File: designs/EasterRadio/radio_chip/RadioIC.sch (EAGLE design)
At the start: 28 parts, among them Q1 2SC3838T146, Y1 32.768kHz crystal

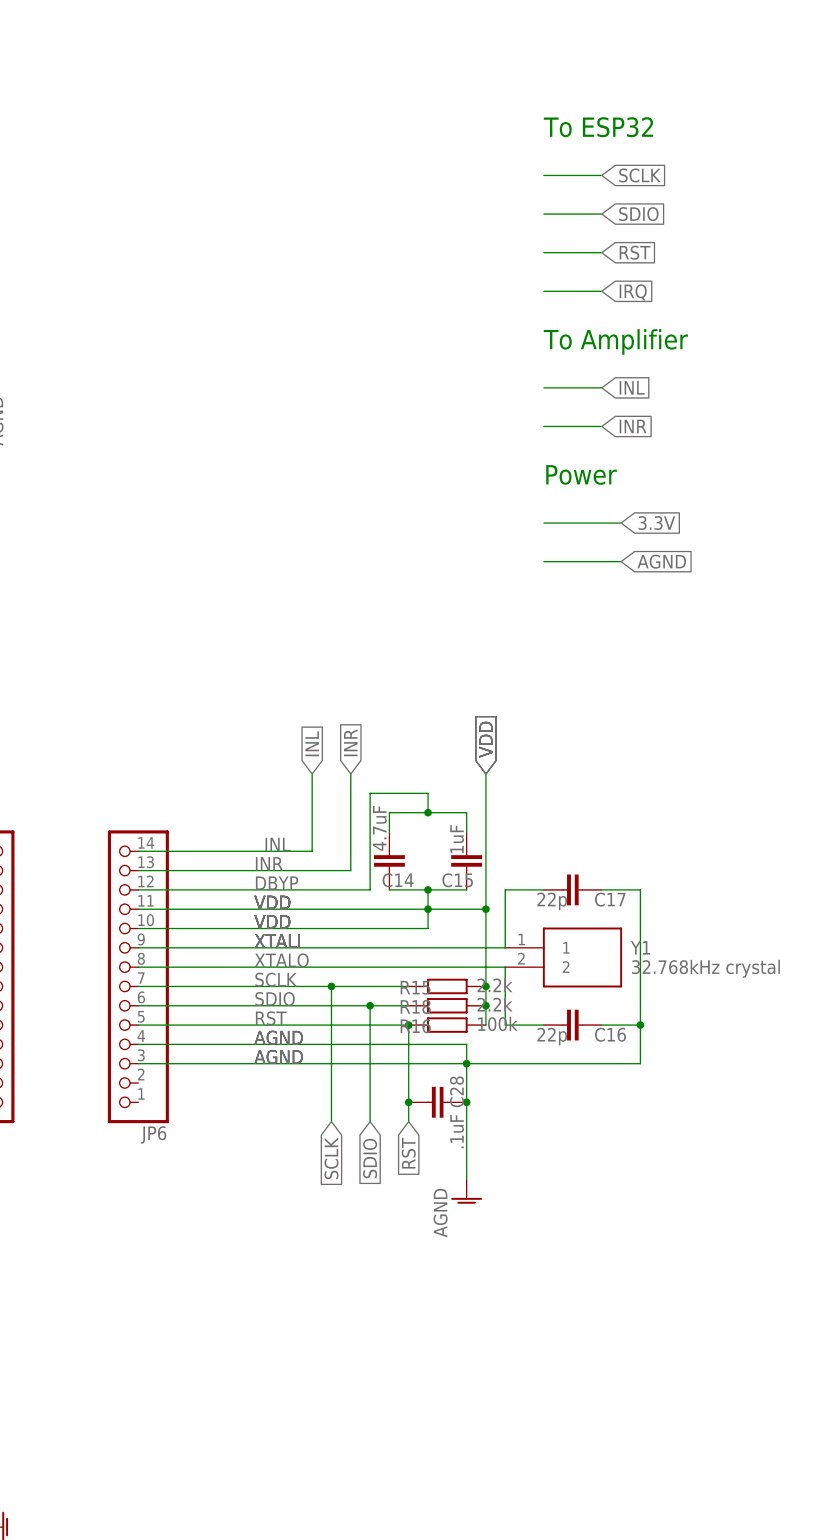
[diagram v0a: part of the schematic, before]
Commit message: changed radio IC
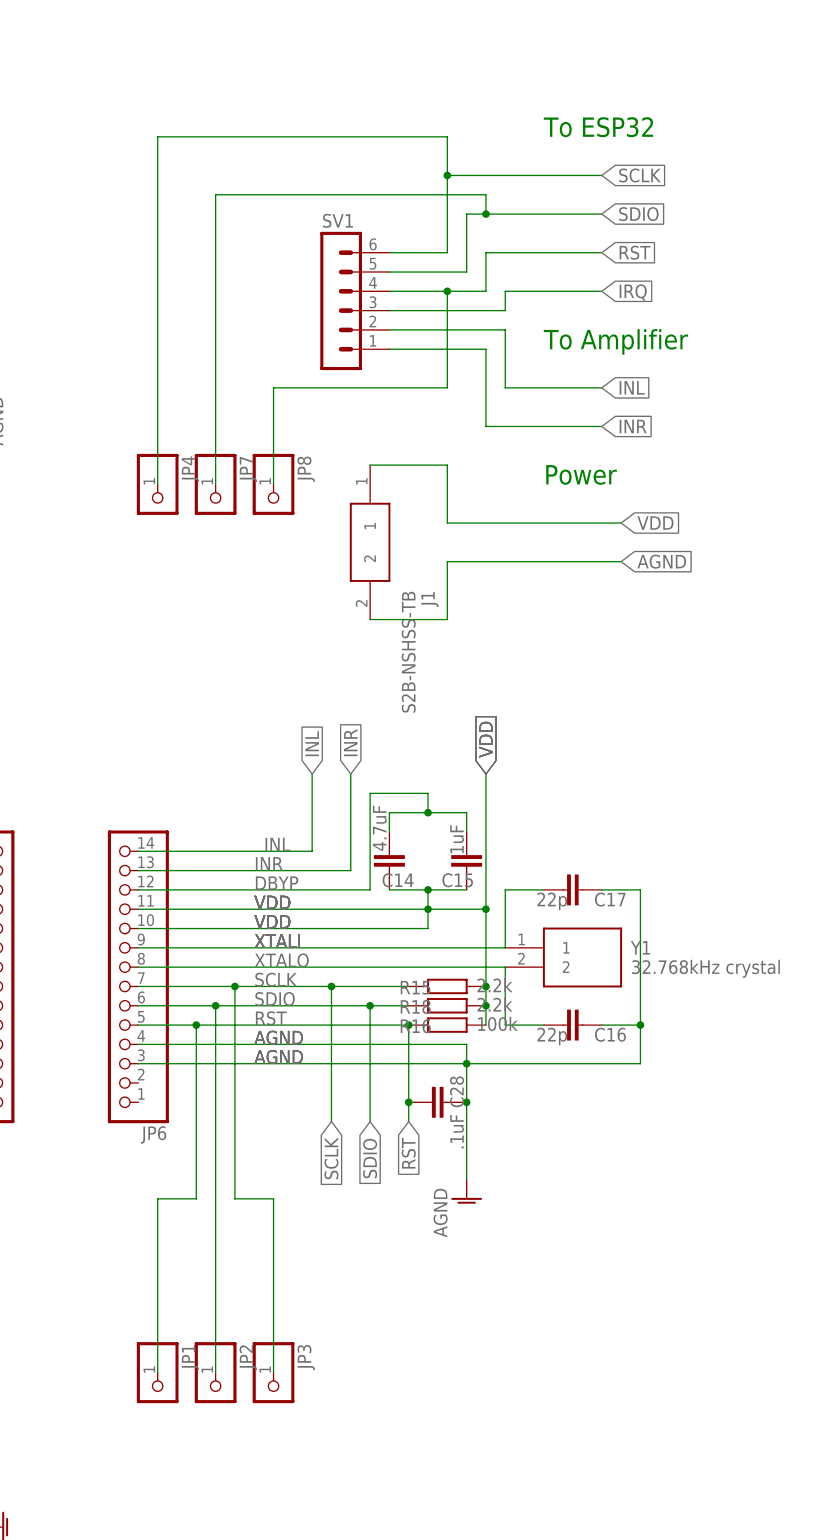
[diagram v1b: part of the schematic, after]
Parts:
- added J1: S2B-NSHSS-TB, CommonParts:S2B-NSHSS-TB
- added JP1, JP2, JP3, JP4, JP7, JP8: (no value), pinhead:PINHD-1X1
- added SV1: (no value), con-lstb:MA06-1
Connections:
- net AGND: now also J1.2
- net INL: now also SV1.2
- net INR: now also SV1.1
- net IRQ: now also SV1.3
- net RST: now also JP1.1, JP8.1, SV1.4
- net SCLK: now also JP3.1, JP4.1, SV1.6
- net SDIO: now also JP2.1, JP7.1, SV1.5
- net VDD: now also J1.1

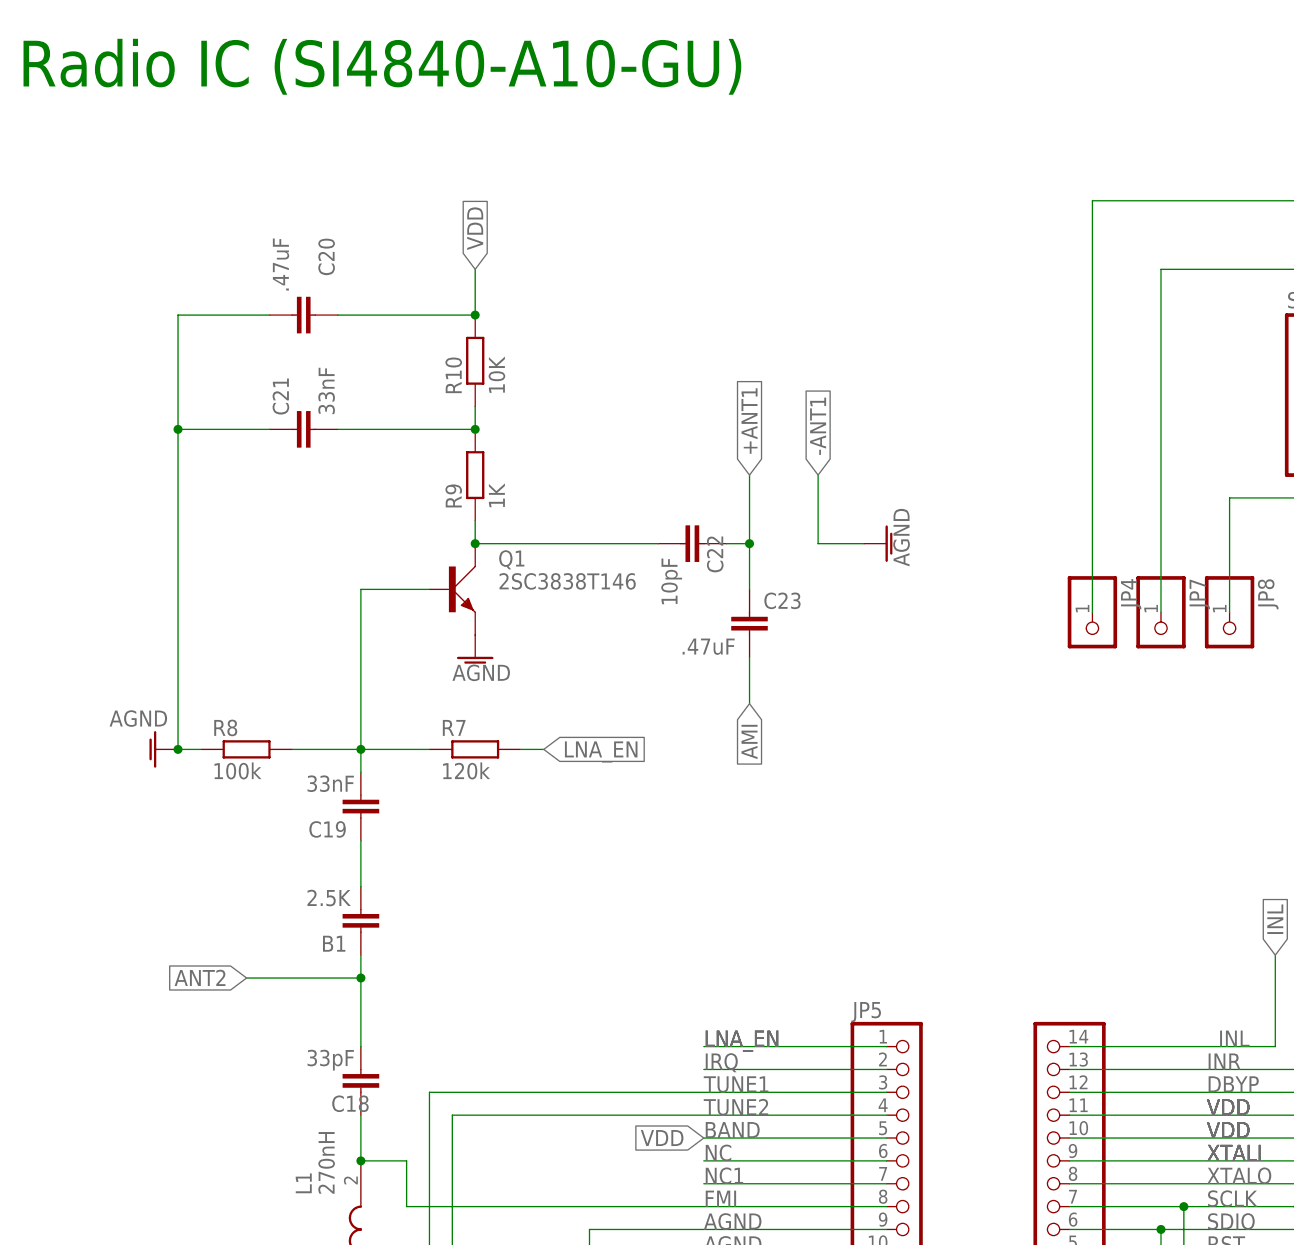
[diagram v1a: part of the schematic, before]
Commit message: changed radio IC
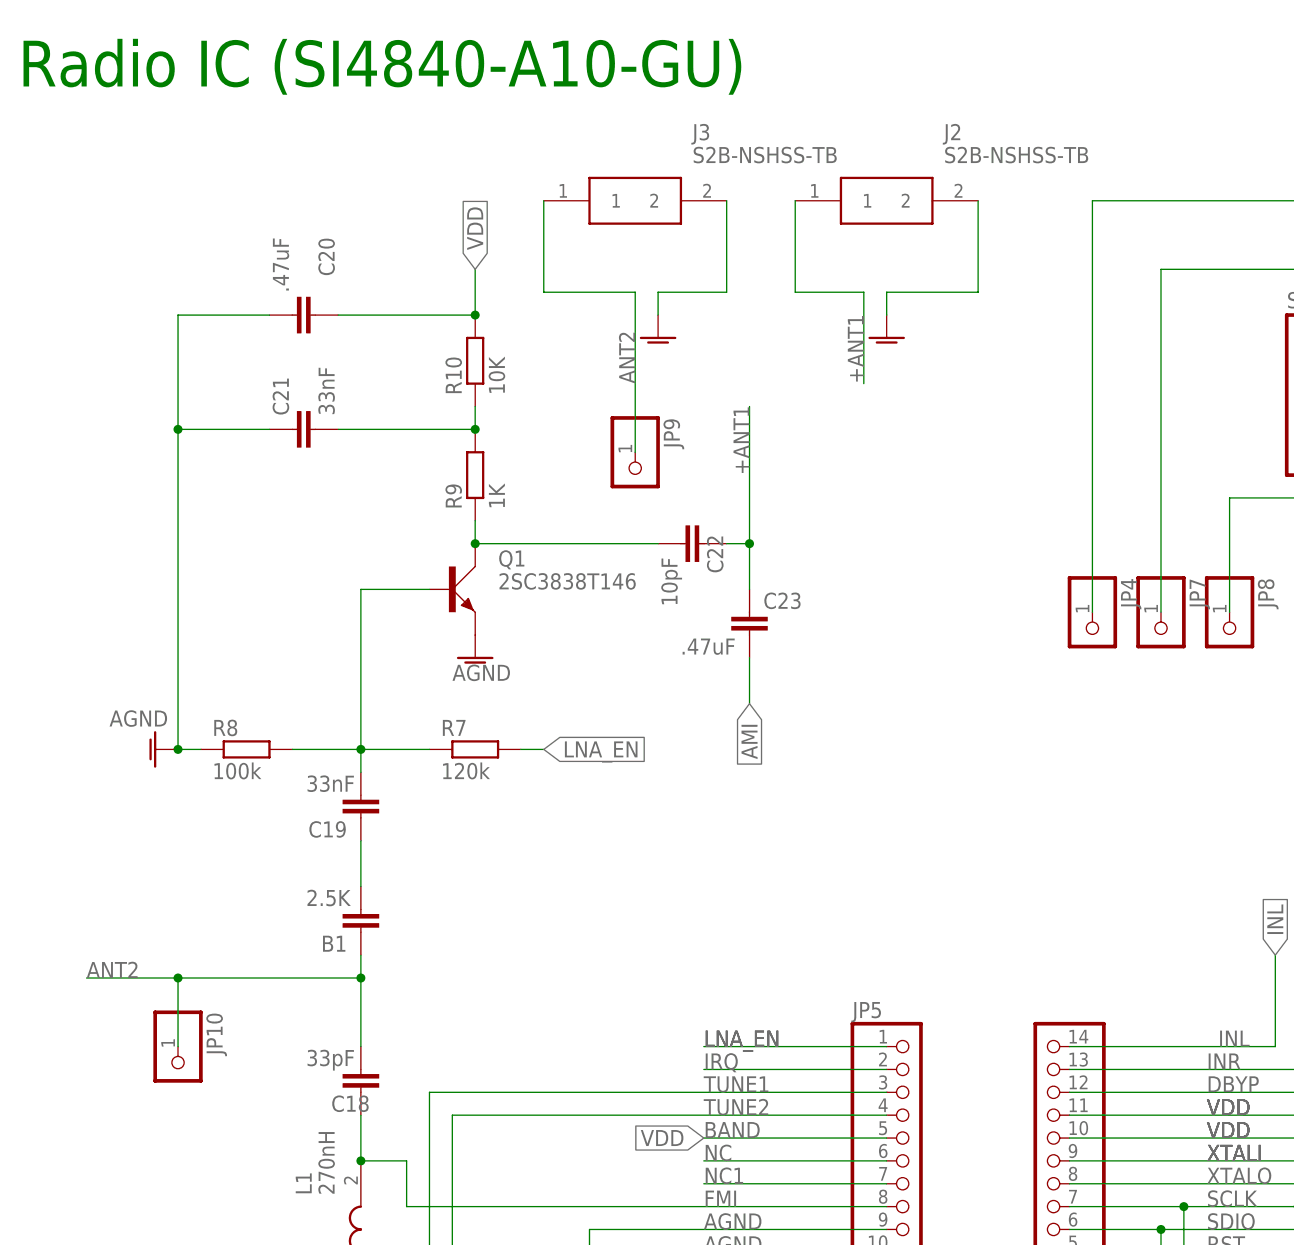
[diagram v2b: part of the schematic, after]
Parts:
- added J2, J3: S2B-NSHSS-TB, CommonParts:S2B-NSHSS-TB
- added JP10, JP9: (no value), pinhead:PINHD-1X1
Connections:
- net +ANT1: now also J2.1
- net AGND: now also J2.2, J3.2
- net ANT2: now also J3.1, JP10.1, JP9.1
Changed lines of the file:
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@@
 <part name="C21" library="MouserUseful" deviceset="CNC5L1X7R1C106K160AE" device="C1206" package3d_urn="urn:adsk.eagle:package:23618/2" value="33nF"/>
 <part name="C22" library="CommonParts" deviceset="C-EU_805" device="C0805" package3d_urn="urn:adsk.eagle:package:23617/2" value="10pF"/>
-<part name="AGND9" library="supply1" library_urn="urn:adsk.eagle:library:371" deviceset="AGND" device=""/>
 <part name="C23" library="CommonParts" deviceset="C-EU_805" device="C0805" package3d_urn="urn:adsk.eagle:package:23617/2" value=".47uF"/>
 <part name="VR1" library="MouserUseful" deviceset="RK09D113BF25B15" device=""/>
@@
 <part name="JP7" library="pinhead" library_urn="urn:adsk.eagle:library:325" deviceset="PINHD-1X1" device="" package3d_urn="urn:adsk.eagle:package:22485/2"/>
 <part name="JP8" library="pinhead" library_urn="urn:adsk.eagle:library:325" deviceset="PINHD-1X1" device="" package3d_urn="urn:adsk.eagle:package:22485/2"/>
+<part name="AGND1" library="supply1" library_urn="urn:adsk.eagle:library:371" deviceset="AGND" device=""/>
+<part name="AGND9" library="supply1" library_urn="urn:adsk.eagle:library:371" deviceset="AGND" device=""/>
+<part name="J2" library="CommonParts" deviceset="S2B-NSHSS-TB" device=""/>
+<part name="J3" library="CommonParts" deviceset="S2B-NSHSS-TB" device=""/>
+<part name="JP9" library="pinhead" library_urn="urn:adsk.eagle:library:325" deviceset="PINHD-1X1" device="" package3d_urn="urn:adsk.eagle:package:22485/2"/>
+<part name="JP10" library="pinhead" library_urn="urn:adsk.eagle:library:325" deviceset="PINHD-1X1" device="" package3d_urn="urn:adsk.eagle:package:22485/2"/>
 </parts>
 <sheets>
@@
 <attribute name="VALUE" x="71.501" y="158.496" size="1.778" layer="96" rot="R270"/>
 </instance>
-<instance part="AGND9" gate="VR1" x="96.52" y="160.02" smashed="yes" rot="R90">
-<attribute name="VALUE" x="99.06" y="157.48" size="1.778" layer="96" rot="R90"/>
-</instance>
 <instance part="C23" gate="G$1" x="81.28" y="152.4" smashed="yes">
 <attribute name="NAME" x="82.804" y="152.781" size="1.778" layer="95"/>
@@
 <attribute name="NAME" x="137.795" y="156.21" size="1.778" layer="95" rot="R270"/>
 <attribute name="VALUE" x="129.54" y="156.21" size="1.778" layer="96" rot="R270"/>
+</instance>
+<instance part="AGND1" gate="VR1" x="71.12" y="182.88" smashed="yes"/>
+<instance part="AGND9" gate="VR1" x="96.52" y="182.88" smashed="yes"/>
+<instance part="J2" gate="G$1" x="86.36" y="198.12" smashed="yes">
+<attribute name="NAME" x="102.87" y="205.74" size="1.778" layer="95" align="center-left"/>
+<attribute name="VALUE" x="102.87" y="203.2" size="1.778" layer="96" align="center-left"/>
+</instance>
+<instance part="J3" gate="G$1" x="58.42" y="198.12" smashed="yes">
+<attribute name="NAME" x="74.93" y="205.74" size="1.778" layer="95" align="center-left"/>
+<attribute name="VALUE" x="74.93" y="203.2" size="1.778" layer="96" align="center-left"/>
+</instance>
+<instance part="JP9" gate="G$1" x="68.58" y="167.64" smashed="yes" rot="R270">
+<attribute name="NAME" x="71.755" y="173.99" size="1.778" layer="95" rot="R270"/>
+<attribute name="VALUE" x="63.5" y="173.99" size="1.778" layer="96" rot="R270"/>
+</instance>
+<instance part="JP10" gate="G$1" x="17.78" y="101.6" smashed="yes" rot="R270">
+<attribute name="NAME" x="20.955" y="107.95" size="1.778" layer="95" rot="R270"/>
+<attribute name="VALUE" x="12.7" y="107.95" size="1.778" layer="96" rot="R270"/>
 </instance>
 </instances>
@@
 <wire x1="157.48" y1="134.62" x2="147.32" y2="134.62" width="0.1524" layer="91"/>
 </segment>
+<segment>
+<wire x1="71.12" y1="185.42" x2="71.12" y2="187.96" width="0.1524" layer="91"/>
+<pinref part="AGND1" gate="VR1" pin="AGND"/>
+<wire x1="71.12" y1="187.96" x2="78.74" y2="187.96" width="0.1524" layer="91"/>
+<pinref part="J3" gate="G$1" pin="2"/>
+<wire x1="78.74" y1="187.96" x2="78.74" y2="198.12" width="0.1524" layer="91"/>
+</segment>
+<segment>
+<pinref part="AGND9" gate="VR1" pin="AGND"/>
+<wire x1="96.52" y1="185.42" x2="96.52" y2="187.96" width="0.1524" layer="91"/>
+<pinref part="J2" gate="G$1" pin="2"/>
+<wire x1="96.52" y1="187.96" x2="106.68" y2="187.96" width="0.1524" layer="91"/>
+<wire x1="106.68" y1="187.96" x2="106.68" y2="198.12" width="0.1524" layer="91"/>
+</segment>
 </net>
 <net name="LNA_EN" class="0">
@@
 <pinref part="C18" gate="G$1" pin="2"/>
 <wire x1="38.1" y1="104.14" x2="38.1" y2="111.76" width="0.1524" layer="91"/>
-<wire x1="38.1" y1="111.76" x2="25.4" y2="111.76" width="0.1524" layer="91"/>
-<label x="25.4" y="111.76" size="1.778" layer="95" rot="R180" xref="yes"/>
 <pinref part="B1" gate="G$1" pin="1"/>
 <wire x1="38.1" y1="114.3" x2="38.1" y2="111.76" width="0.1524" layer="91"/>
 <junction x="38.1" y="111.76"/>
+<wire x1="38.1" y1="111.76" x2="17.78" y2="111.76" width="0.1524" layer="91"/>
+<label x="7.62" y="111.76" size="1.778" layer="95"/>
+<pinref part="JP10" gate="G$1" pin="1"/>
+<wire x1="17.78" y1="111.76" x2="7.62" y2="111.76" width="0.1524" layer="91"/>
+<wire x1="17.78" y1="104.14" x2="17.78" y2="111.76" width="0.1524" layer="91"/>
+<junction x="17.78" y="111.76"/>
+</segment>
+<segment>
+<wire x1="68.58" y1="187.96" x2="68.58" y2="170.18" width="0.1524" layer="91"/>
+<label x="68.58" y="177.8" size="1.778" layer="95" rot="R90"/>
+<pinref part="J3" gate="G$1" pin="1"/>
+<wire x1="68.58" y1="187.96" x2="58.42" y2="187.96" width="0.1524" layer="91"/>
+<wire x1="58.42" y1="187.96" x2="58.42" y2="198.12" width="0.1524" layer="91"/>
+<pinref part="JP9" gate="G$1" pin="1"/>
 </segment>
 </net>
@@
 </segment>
 </net>
-<net name="+ANT1" class="0">
-<segment>
-<pinref part="C22" gate="G$1" pin="1"/>
-<wire x1="78.74" y1="160.02" x2="81.28" y2="160.02" width="0.1524" layer="91"/>
-<wire x1="81.28" y1="160.02" x2="81.28" y2="167.64" width="0.1524" layer="91"/>
-<label x="81.28" y="167.64" size="1.778" layer="95" rot="R90" xref="yes"/>
-<junction x="81.28" y="160.02"/>
-<wire x1="81.28" y1="160.02" x2="81.28" y2="154.94" width="0.1524" layer="91"/>
-<pinref part="C23" gate="G$1" pin="1"/>
-</segment>
-</net>
-<net name="-ANT1" class="0">
-<segment>
-<wire x1="88.9" y1="167.64" x2="88.9" y2="160.02" width="0.1524" layer="91"/>
-<wire x1="88.9" y1="160.02" x2="93.98" y2="160.02" width="0.1524" layer="91"/>
-<label x="88.9" y="167.64" size="1.778" layer="95" rot="R90" xref="yes"/>
-<pinref part="AGND9" gate="VR1" pin="AGND"/>
-</segment>
-</net>
 <net name="N$9" class="0">
 <segment>
@@
 </segment>
 </net>
+<net name="+ANT1" class="0">
+<segment>
+<wire x1="93.98" y1="187.96" x2="93.98" y2="177.8" width="0.1524" layer="91"/>
+<label x="93.98" y="177.8" size="1.778" layer="95" rot="R90"/>
+<wire x1="93.98" y1="187.96" x2="86.36" y2="187.96" width="0.1524" layer="91"/>
+<pinref part="J2" gate="G$1" pin="1"/>
+<wire x1="86.36" y1="187.96" x2="86.36" y2="198.12" width="0.1524" layer="91"/>
+</segment>
+<segment>
+<pinref part="C23" gate="G$1" pin="1"/>
+<pinref part="C22" gate="G$1" pin="1"/>
+<wire x1="78.74" y1="160.02" x2="81.28" y2="160.02" width="0.1524" layer="91"/>
+<junction x="81.28" y="160.02"/>
+<wire x1="81.28" y1="160.02" x2="81.28" y2="154.94" width="0.1524" layer="91"/>
+<wire x1="81.28" y1="160.02" x2="81.28" y2="175.26" width="0.1524" layer="91"/>
+<label x="81.28" y="167.64" size="1.778" layer="95" rot="R90"/>
+</segment>
+</net>
